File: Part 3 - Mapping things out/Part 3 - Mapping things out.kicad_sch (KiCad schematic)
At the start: 18 parts, among them J1 +5V DC/CP, SW1 POWER, SW2 RESET, U1 74HC14, U2 74HC175

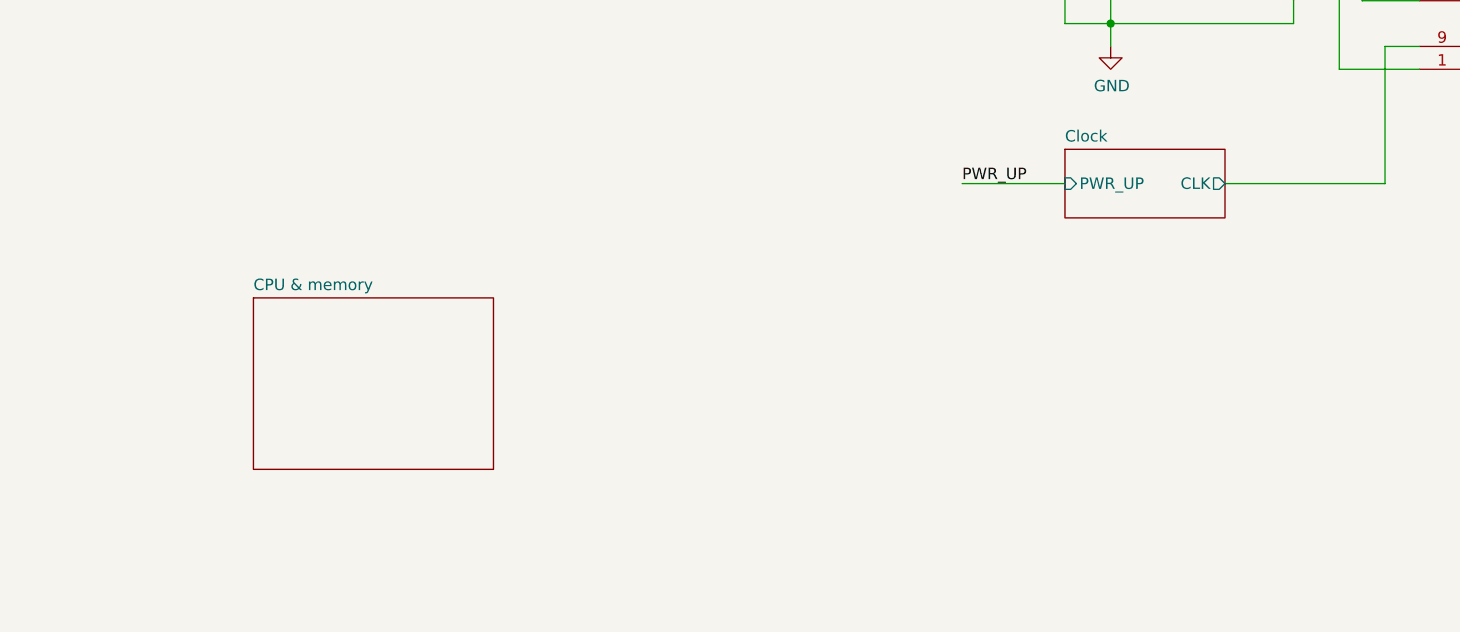
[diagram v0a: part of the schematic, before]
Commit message: Updated glue logic and bank switching
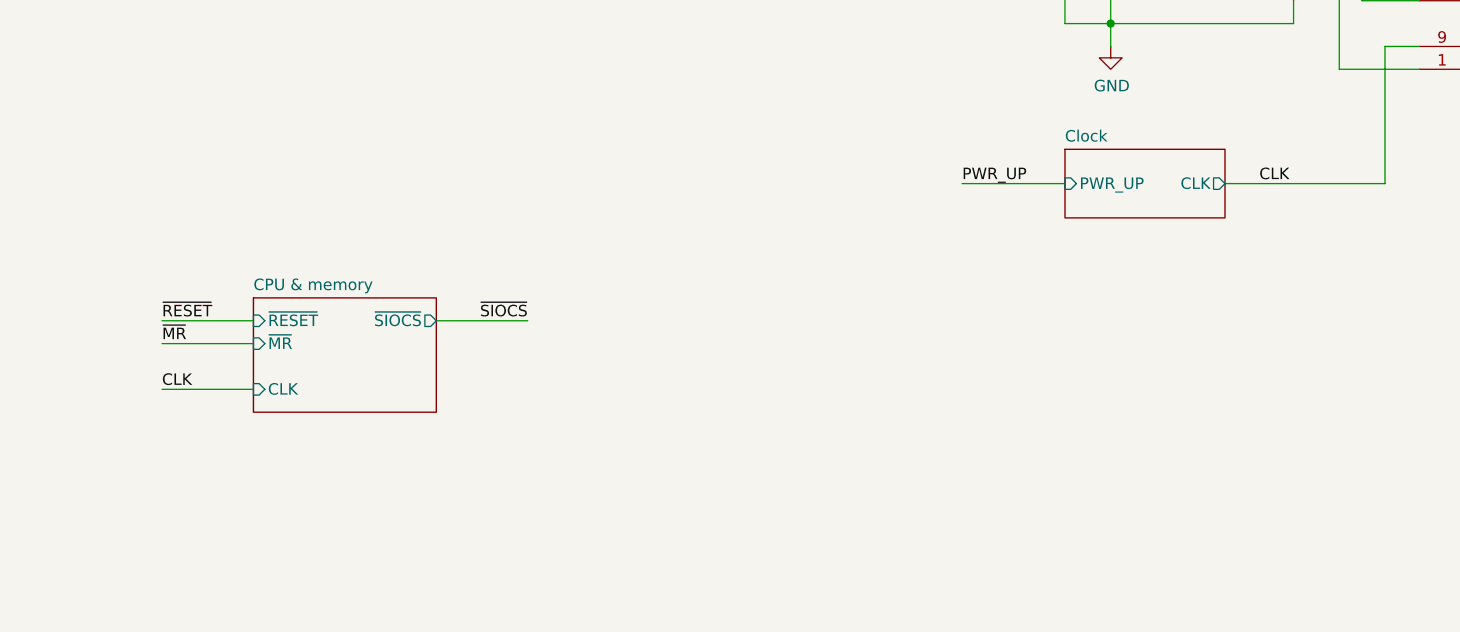
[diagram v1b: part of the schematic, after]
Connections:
- net Clock/CLK renamed CLK
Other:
- sheet CPU & memory ports: added CLK, ~{MR}, ~{RESET}, ~{SIOCS}; removed none

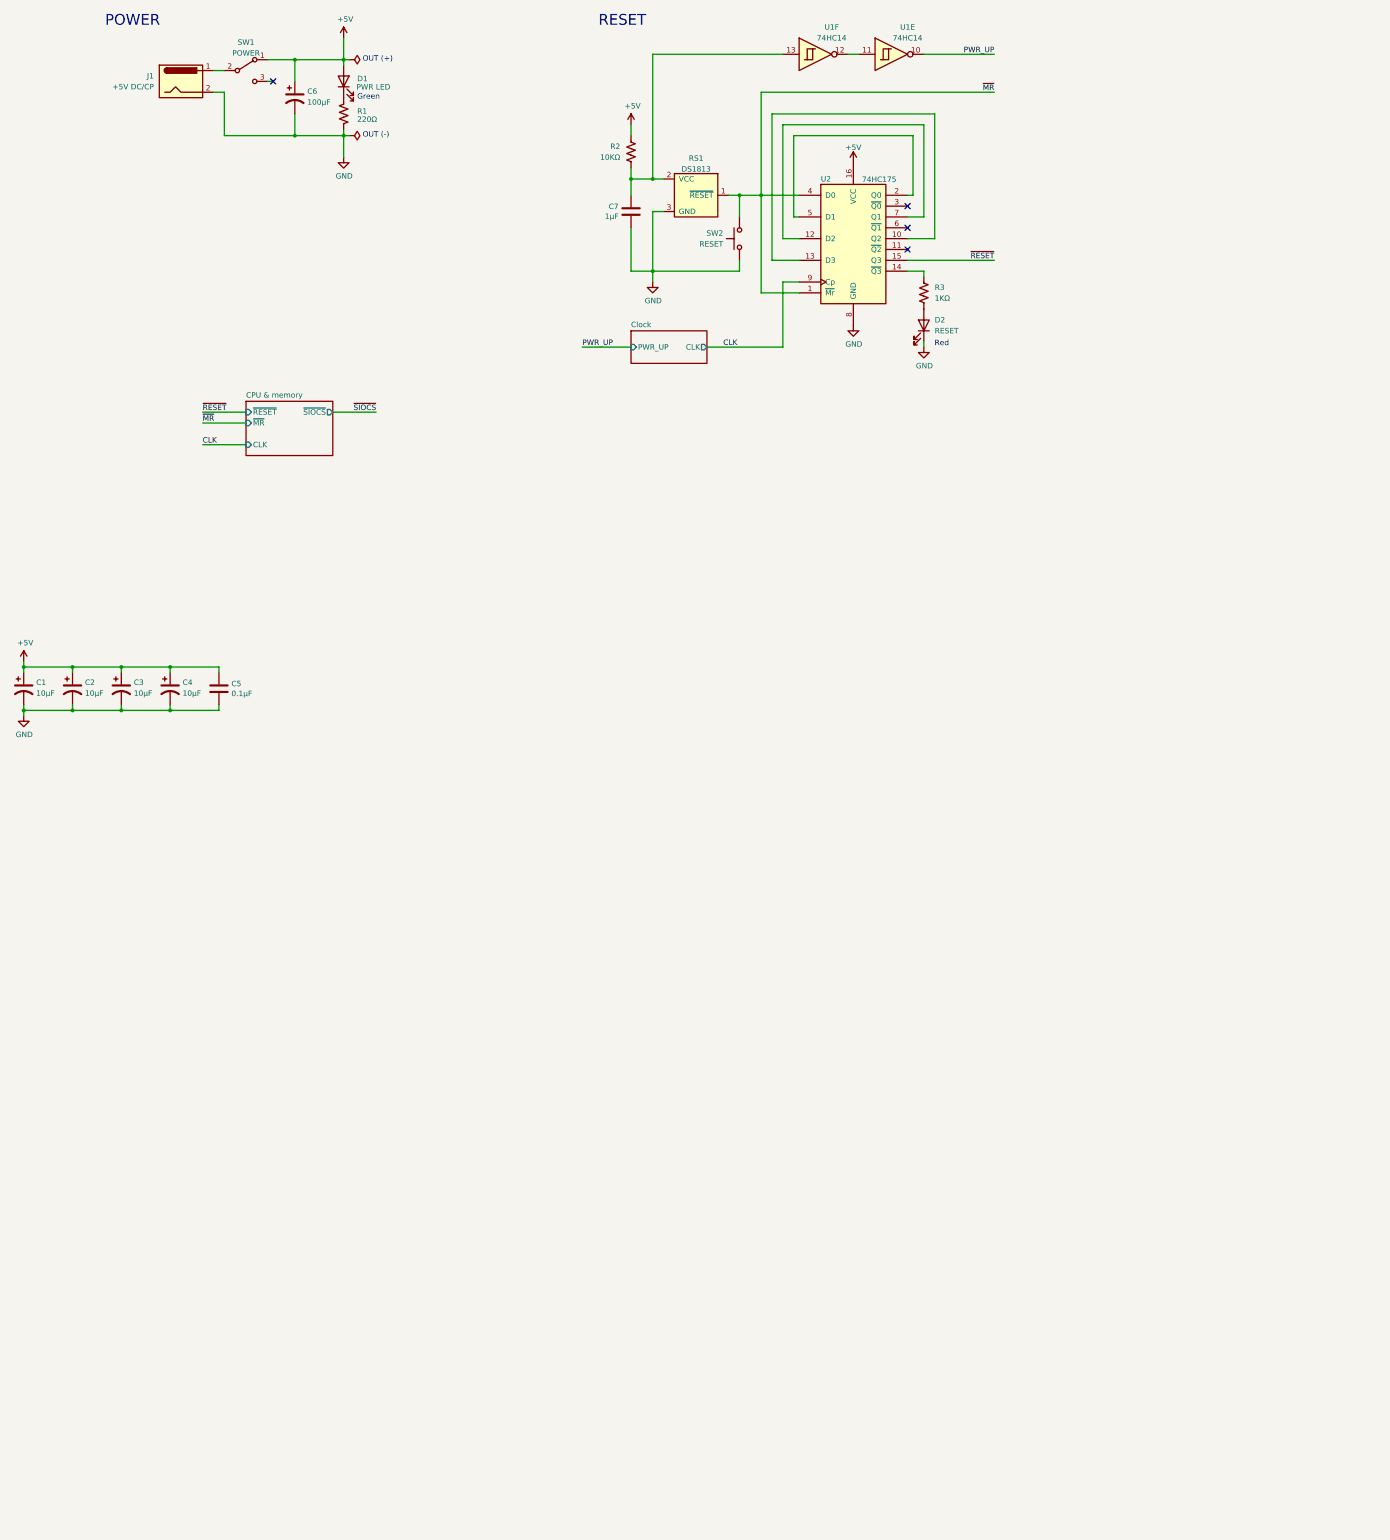
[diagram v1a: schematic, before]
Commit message: Backplane PCB sent out, and experimented with clock options
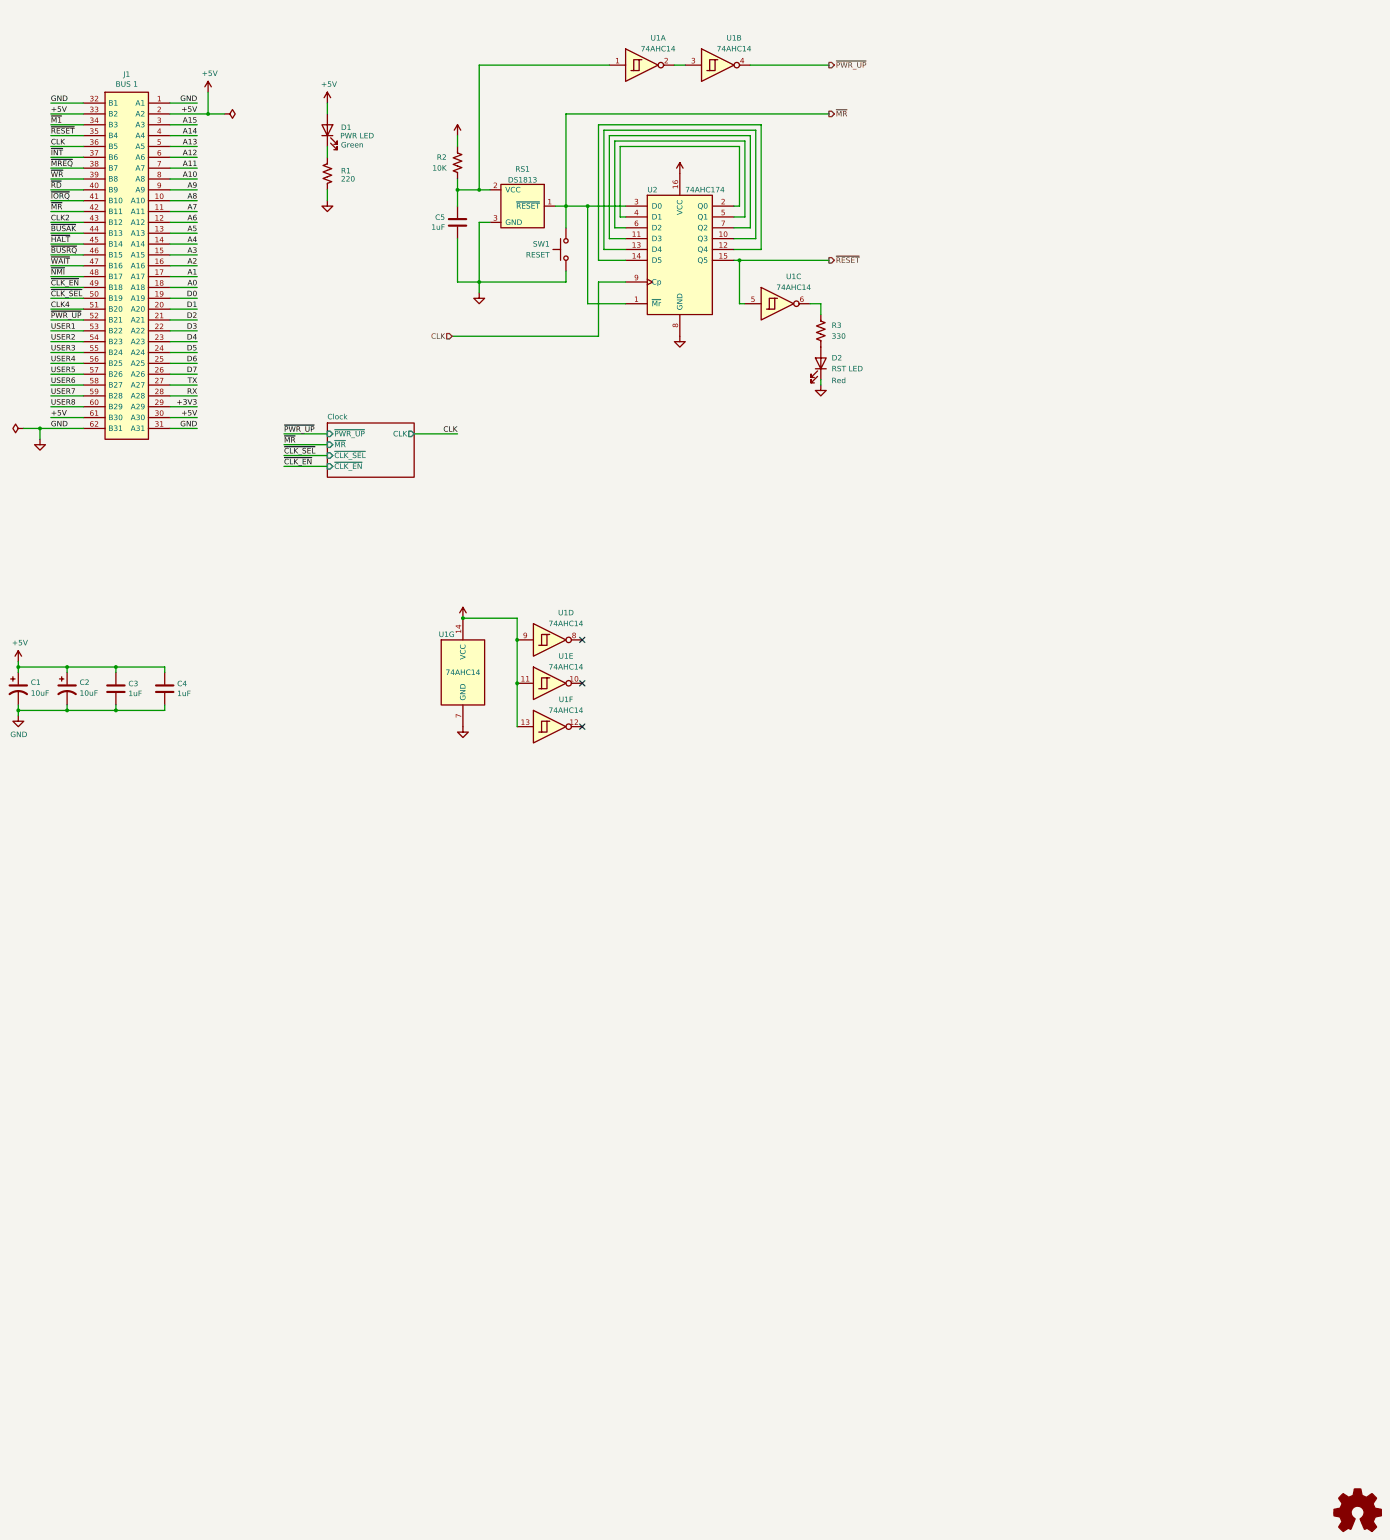
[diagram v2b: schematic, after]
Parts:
- removed C3, C4: 10µF, Capacitor_THT:CP_Radial_D6.3mm_P2.50mm, symbol Device:C_Polarized_US
- removed C6: 100µF, Capacitor_THT:CP_Radial_D8.0mm_P3.80mm, symbol Device:C_Polarized_US
- removed C7: 1µF, Capacitor_THT:C_Disc_D3.0mm_W1.6mm_P2.50mm, symbol Device:C
- removed J1: +5V DC/CP, Connector_BarrelJack:BarrelJack_Horizontal, symbol Connector:Barrel_Jack
- removed SW1: POWER, symbol Switch:SW_SPDT
- removed SW2: RESET, Button_Switch_THT:SW_PUSH_6mm, symbol Switch:SW_Push
- removed U2: 74HC175, Package_DIP:DIP-16_W7.62mm_Socket, symbol 74xx:74LS175
- added C3, C4: 1uF, Capacitor_THT:C_Disc_D3.0mm_W2.0mm_P2.50mm, symbol Device:C
- added J1: BUS 1, 0_Z80_Library:BUS_XT, symbol 0_Z80_Library:ISA_CARD_CONNECTOR
- added SW1: RESET, Button_Switch_THT:SW_PUSH-12mm_Wuerth-430476085716, symbol Switch:SW_Push
- added unit 7 of U1
- added unit 2 of U1
- added unit 1 of U1
- added unit 3 of U1
- added unit 4 of U1
- added U2: 74AHC174, Package_DIP:DIP-16_W7.62mm_Socket, symbol 74xx:74LS174
- C1, C2: value 10µF -> 10uF
- C5: value 0.1µF -> 1uF; footprint Capacitor_THT:C_Disc_D3.0mm_W1.6mm_P2.50mm -> Capacitor_THT:C_Disc_D3.0mm_W2.0mm_P2.50mm
- D2: value RESET -> RST LED; footprint LED_THT:LED_D3.0mm -> LED_THT:LED_D3.0mm_Horizontal_O1.27mm_Z2.0mm_Clear
- R1: value 220Ω -> 220
- R2: value 10KΩ -> 10K
- R3: value 1KΩ -> 330
- U1: value 74HC14 -> 74AHC14
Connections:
- net +5V: now also U1.11, U1.13, C3.1, C4.1, J1.2 (A2), J1.30 (A30), J1.33 (B2), J1.61 (B30), U1.14 (VCC), U1.9, U2.16 (VCC); no longer C5.1
- net CLK: now also J1.36 (B5), U2.9 (Cp)
- net GND: now also C3.2, C4.2, J1.1 (A1), J1.31 (A31), J1.32 (B1), J1.62 (B31), SW1.2, U1.7 (GND), U2.8 (GND)
- net ~{MR}: now also J1.42 (B11), SW1.1, U2.1 (~{Mr}), U2.3 (D0)
- net ~{RESET}: now also J1.35 (B4), U1.5, U2.15 (Q5)
- net at R2.1, RS1.2 (VCC): now also C5.1, U1.1; no longer U1.13
- net at R3.1: now also U1.6
- net at U1.12: no longer U1.11
- net PWR_UP: no longer names the net of U1.10
- new net: U2.10 (Q3), U2.13 (D4)
- new net: U2.11 (D3), U2.7 (Q2)
- new net: U2.12 (Q4), U2.14 (D5)
- new net: U2.2 (Q0), U2.4 (D1)
- new net: U2.5 (Q1), U2.6 (D2)
- new net: U1.2, U1.3
- new net +3V3: J1.29 (A29)
- new net A0: J1.18 (A18)
- new net A1: J1.17 (A17)
- new net A10: J1.8 (A8)
- new net A11: J1.7 (A7)
- new net A12: J1.6 (A6)
- new net A13: J1.5 (A5)
- new net A14: J1.4 (A4)
- new net A15: J1.3 (A3)
- new net A2: J1.16 (A16)
- new net A3: J1.15 (A15)
- new net A4: J1.14 (A14)
- new net A5: J1.13 (A13)
- new net A6: J1.12 (A12)
- new net A7: J1.11 (A11)
- new net A8: J1.10 (A10)
- new net A9: J1.9 (A9)
- new net CLK2: J1.43 (B12)
- new net CLK4: J1.51 (B20)
- new net D0: J1.19 (A19)
- new net D1: J1.20 (A20)
- new net D2: J1.21 (A21)
- new net D3: J1.22 (A22)
- new net D4: J1.23 (A23)
- new net D5: J1.24 (A24)
- new net D6: J1.25 (A25)
- new net D7: J1.26 (A26)
- new net RX: J1.28 (A28)
- new net TX: J1.27 (A27)
- new net USER1: J1.53 (B22)
- new net USER2: J1.54 (B23)
- new net USER3: J1.55 (B24)
- new net USER4: J1.56 (B25)
- new net USER5: J1.57 (B26)
- new net USER6: J1.58 (B27)
- new net USER7: J1.59 (B28)
- new net USER8: J1.60 (B29)
- new net ~{BUSAK}: J1.44 (B13)
- new net ~{BUSRQ}: J1.46 (B15)
- new net ~{CLK_EN}: J1.49 (B18)
- new net ~{CLK_SEL}: J1.50 (B19)
- new net ~{HALT}: J1.45 (B14)
- new net ~{INT}: J1.37 (B6)
- new net ~{IORQ}: J1.41 (B10)
- new net ~{M1}: J1.34 (B3)
- new net ~{MREQ}: J1.38 (B7)
- new net ~{NMI}: J1.48 (B17)
- new net ~{PWR_UP}: J1.52 (B21), U1.4
- new net ~{RD}: J1.40 (B9)
- new net ~{WAIT}: J1.47 (B16)
- new net ~{WR}: J1.39 (B8)
- no-connect marks 4 -> 3
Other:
- removed sheet CPU & memory
- sheet Clock ports: added ~{CLK_EN}, ~{CLK_SEL}, ~{MR}, ~{PWR_UP}; removed PWR_UP
- note removed: "OUT (+)"
- note removed: "OUT (-)"
- note removed: "POWER"
- note removed: "RESET"
- company: Frederic Segard - aka: The Micro Hobbyist -> Frédéric Segard
- title: Power and clock -> Micro Hobbyist's Z80 Homebrew Project
